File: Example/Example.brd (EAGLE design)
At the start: 86 x 54 mm, 25 parts, among them IC2 74LS02D, IC3 74LS02D, U1 CD4017

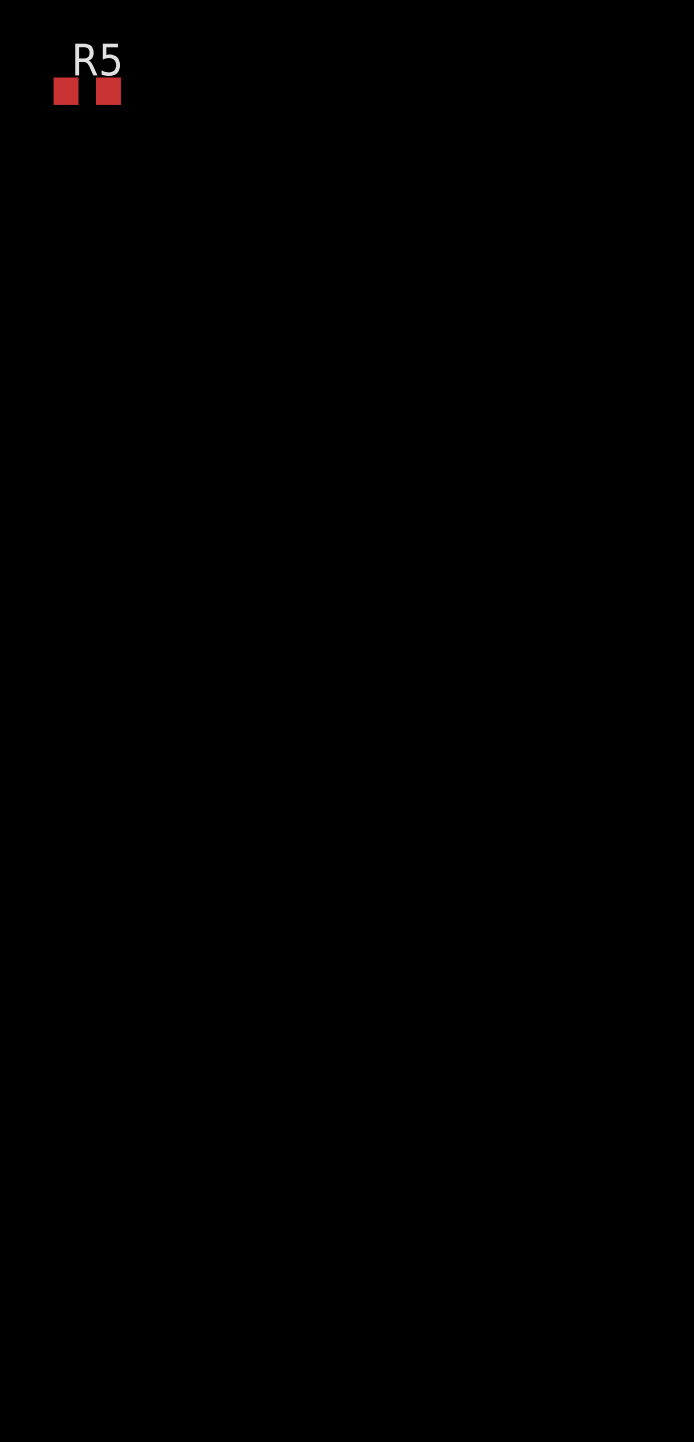
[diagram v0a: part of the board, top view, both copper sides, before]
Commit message: decade counter
added clocks and EN
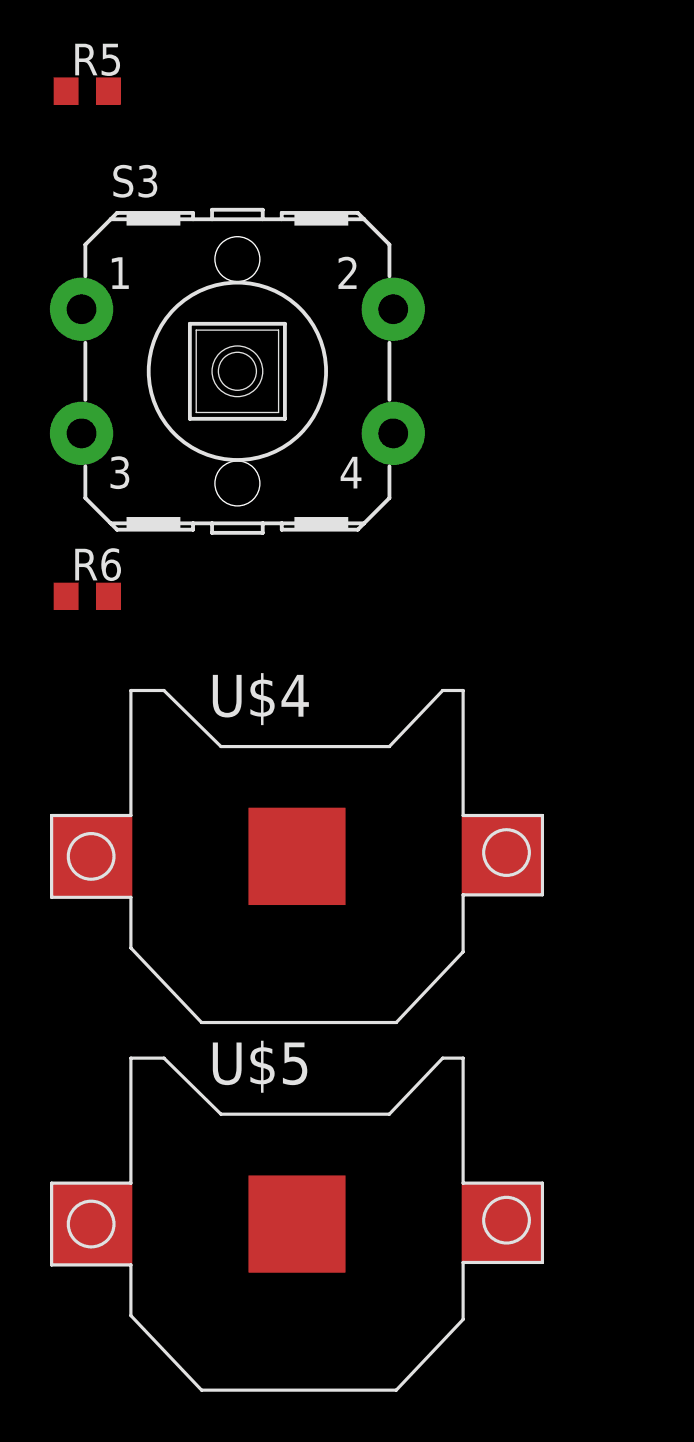
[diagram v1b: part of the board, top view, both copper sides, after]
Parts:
- added R6: 220, rcl:R0603
- added S3: (no value), adafruit:B3F-40XX-ROUND
- added U$4, U$5: (no value), adafruit:CR1220-SMD
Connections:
- new net N$1: R6.2, S3.2, U1.14
- net GND: now also R6.1, U$4.-, U$5.-, U1.13
- net VCC: now also U$4.+$1, U$5.+$1
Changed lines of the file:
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@@
 <attribute name="VALUE" x="-30.415" y="-147.805" size="1.27" layer="27"/>
+</element>
+<element name="S3" library="adafruit" library_urn="urn:adsk.eagle:library:420" package="B3F-40XX-ROUND" package3d_urn="urn:adsk.eagle:package:6240926/1" value="" x="-23.76" y="-157.13" smashed="yes">
+<attribute name="NAME" x="-28.84" y="-150.145" size="1.27" layer="25" ratio="10"/>
+<attribute name="VALUE" x="-26.935" y="-162.21" size="1.27" layer="27" ratio="10"/>
+</element>
+<element name="R6" library="rcl" library_urn="urn:adsk.eagle:library:334" package="R0603" package3d_urn="urn:adsk.eagle:package:23555/3" value="220" x="-29.78" y="-166.15" smashed="yes">
+<attribute name="NAME" x="-30.415" y="-165.515" size="1.27" layer="25"/>
+<attribute name="POPULARITY" value="77" x="-29.78" y="-166.15" size="1.778" layer="27" display="off"/>
+<attribute name="SPICEPREFIX" value="R" x="-29.78" y="-166.15" size="1.778" layer="27" display="off"/>
+<attribute name="VALUE" x="-30.415" y="-168.055" size="1.27" layer="27"/>
+</element>
+<element name="U$4" library="adafruit" library_urn="urn:adsk.eagle:library:420" package="CR1220-SMD" package3d_urn="urn:adsk.eagle:package:6240665/1" value="" x="-21.37" y="-176.58" smashed="yes">
+<attribute name="NAME" x="-24.926" y="-170.978" size="1.6764" layer="25" font="vector"/>
+<attribute name="VALUE" x="-25.688" y="-181.13" size="1.6764" layer="27" font="vector"/>
+</element>
+<element name="U$5" library="adafruit" library_urn="urn:adsk.eagle:library:420" package="CR1220-SMD" package3d_urn="urn:adsk.eagle:package:6240665/1" value="" x="-21.37" y="-191.32" smashed="yes">
+<attribute name="NAME" x="-24.926" y="-185.718" size="1.6764" layer="25" font="vector"/>
+<attribute name="VALUE" x="-25.688" y="-195.87" size="1.6764" layer="27" font="vector"/>
 </element>
 </elements>
@@
 <contactref element="R4" pad="1"/>
 <contactref element="R5" pad="1"/>
+<contactref element="R6" pad="1"/>
+<contactref element="U$4" pad="-"/>
+<contactref element="U$5" pad="-"/>
+<contactref element="U1" pad="13"/>
+<wire x1="-21.37" y1="-176.58" x2="-21.37" y2="-191.32" width="0" layer="19" extent="1-1"/>
+<wire x1="-30.63" y1="-166.15" x2="-21.37" y2="-176.58" width="0" layer="19" extent="1-1"/>
+<wire x1="-30.63" y1="-145.9" x2="-30.63" y2="-166.15" width="0" layer="19" extent="1-1"/>
 <wire x1="-30.63" y1="-141.02" x2="-30.63" y2="-145.9" width="0" layer="19" extent="1-1"/>
-<wire x1="-21.37" y1="-79.78" x2="-30.63" y2="-141.02" width="0" layer="19" extent="1-1"/>
+<wire x1="-20.84" y1="-87.32" x2="-30.63" y2="-141.02" width="0" layer="19" extent="1-1"/>
+<wire x1="-21.37" y1="-79.78" x2="-20.84" y2="-87.32" width="0" layer="19" extent="1-1"/>
 <wire x1="-30.63" y1="-70.74" x2="-21.37" y2="-79.78" width="0" layer="19" extent="1-1"/>
 <wire x1="-30.63" y1="-67.26" x2="-30.63" y2="-70.74" width="0" layer="19" extent="1-1"/>
@@
 <contactref element="U$1" pad="+$1"/>
 <contactref element="U$3" pad="+$1"/>
+<contactref element="U$4" pad="+$1"/>
+<contactref element="U$5" pad="+$1"/>
+<wire x1="-29.57" y1="-176.58" x2="-29.57" y2="-191.32" width="0" layer="19" extent="1-1"/>
+<wire x1="-29.57" y1="-79.78" x2="-29.57" y2="-176.58" width="0" layer="19" extent="1-1"/>
 <wire x1="-30.0084" y1="-60.7292" x2="-29.57" y2="-79.78" width="0" layer="19" extent="1-1"/>
 <wire x1="-14.18" y1="-29.9966" x2="-30.0084" y2="-60.7292" width="0" layer="19" extent="1-1"/>
@@
 <wire x1="-25.92" y1="-87.32" x2="-28.93" y2="-145.9" width="0" layer="19" extent="1-1"/>
 </signal>
+<signal name="N$1">
+<contactref element="S3" pad="2"/>
+<contactref element="R6" pad="2"/>
+<contactref element="U1" pad="14"/>
+<wire x1="-17.5116" y1="-154.6408" x2="-28.93" y2="-166.15" width="0" layer="19" extent="1-1"/>
+<wire x1="-23.38" y1="-87.32" x2="-17.5116" y2="-154.6408" width="0" layer="19" extent="1-1"/>
+</signal>
 </signals>

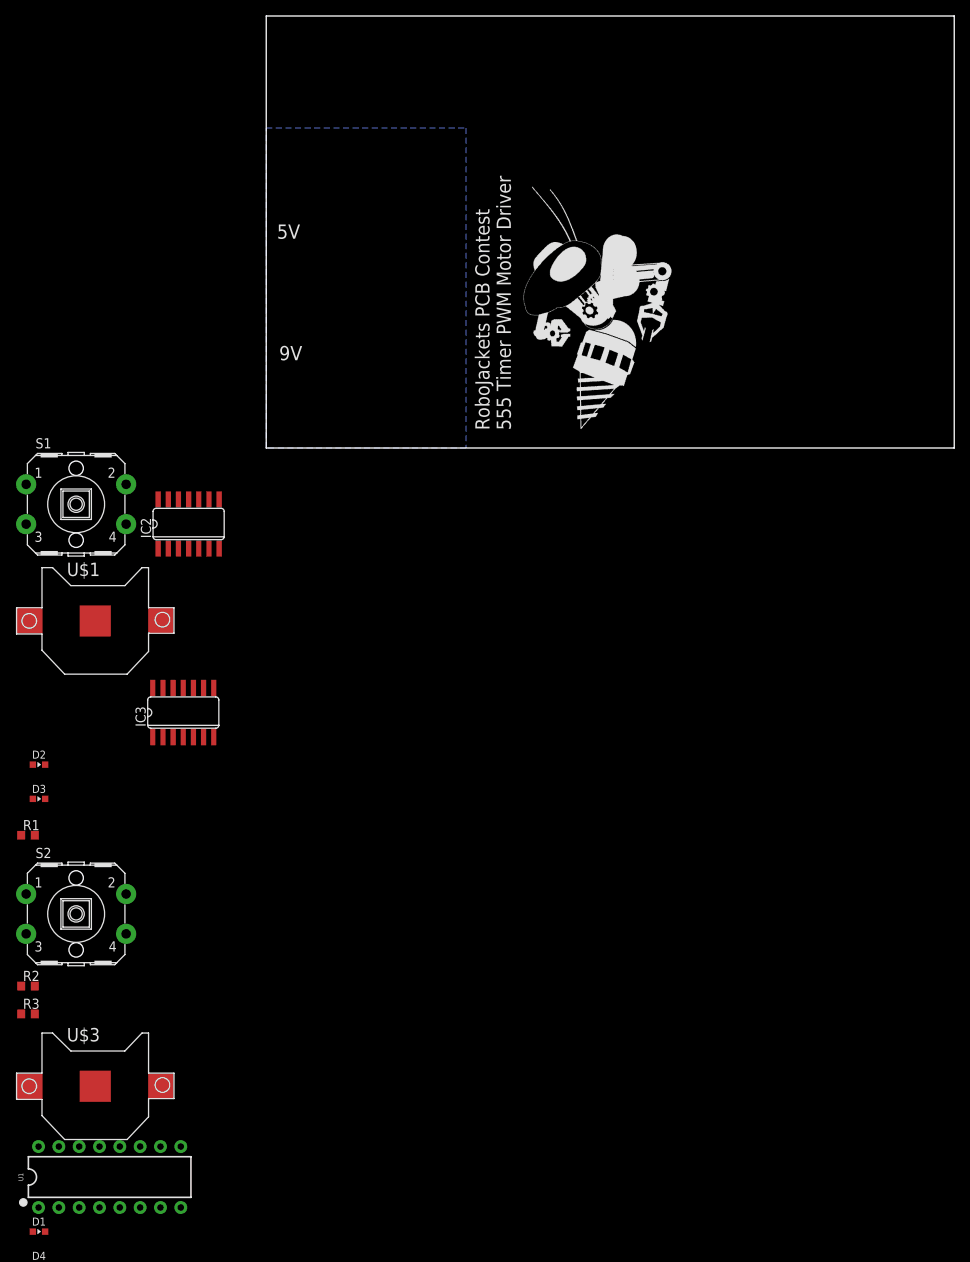
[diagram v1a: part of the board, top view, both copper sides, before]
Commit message: Fixed multiple NOR gate issue
Removed IC3A from the schematic
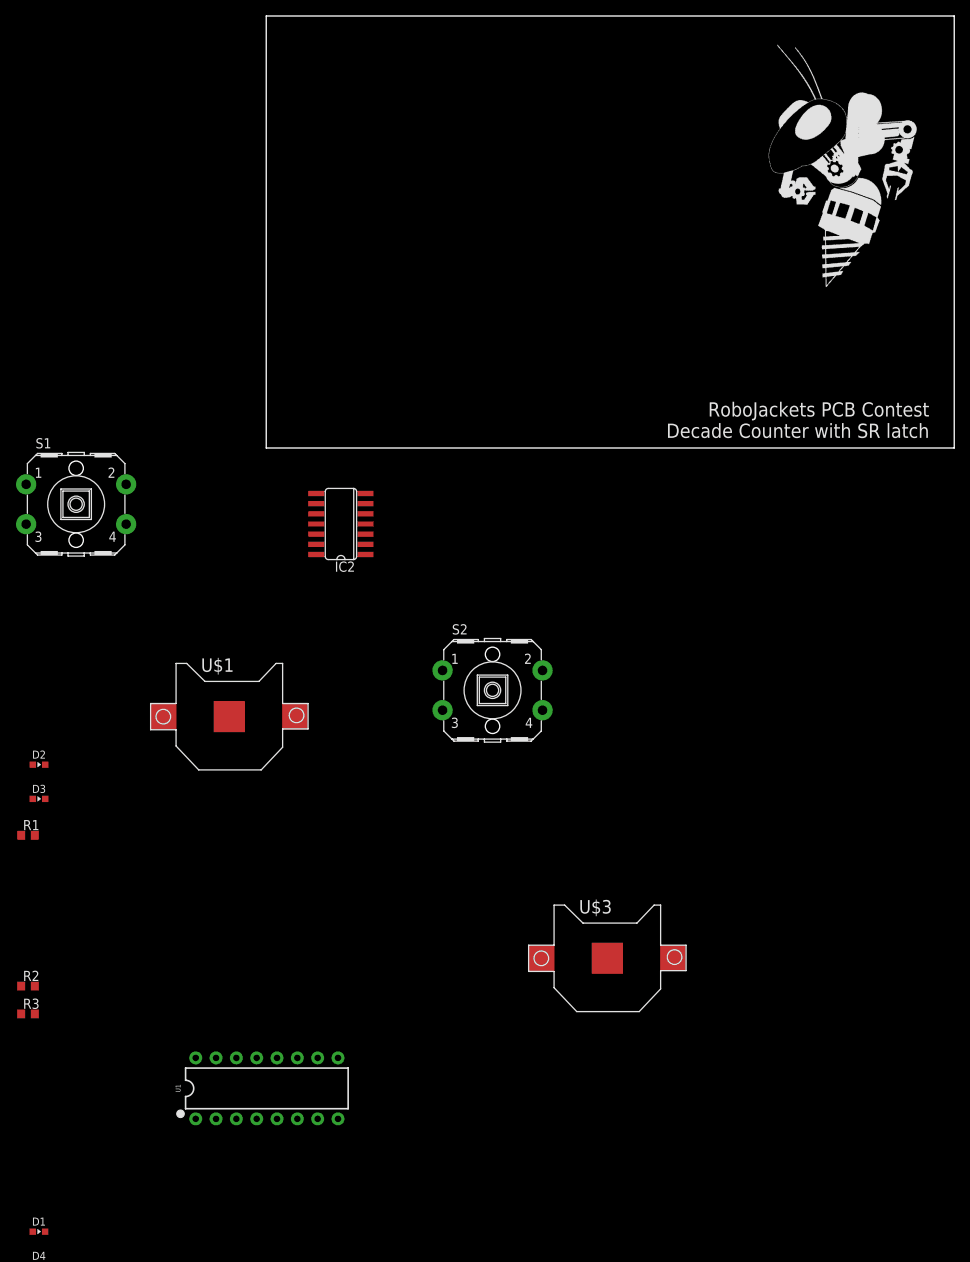
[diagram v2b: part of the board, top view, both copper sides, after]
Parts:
- removed IC3: 74LS02D, 74xx-us:SO14
- moved U$3 66.0 mm to (42.6, -63.8)
- moved S2 59.1 mm to (28.3, -30.3)
- moved U$2 35.4 mm to (69.9, 20.1)
- moved U1 22.6 mm to (0.08, -80.0)
- moved U$1 20.6 mm to (-4.61, -33.6)
- moved IC2 19.0 mm to (9.34, -9.50), turned to 90 degrees
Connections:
- removed net N$7: IC2.5
- removed net N$8: IC2.4
- removed net N$9: IC2.6
- net GND: no longer IC3.7
- net Q: now also IC2.5; no longer IC3.2
- net QNOT: now also IC2.4; no longer IC3.1
- net S: now also IC2.6; no longer IC3.3
- net VCC: no longer IC3.14
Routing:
- removed copper zone on layer 16, net GND
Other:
- board text added: "RoboJackets PCB Contest Decade Counter with SR latch"
- board text removed: "5V"
- board text removed: "9V"
- board text removed: "RoboJackets PCB Contest 555 Timer PWM Motor Driver"

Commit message: placed items on board
i placed everything on the board except for battery holders
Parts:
- removed D2: YELLOW, RoboJackets-LEDs:LED0603
- moved R6 192.5 mm to (45.6, 11.0)
- moved S3 178.0 mm to (31.9, 11.9)
- moved R5 177.5 mm to (45.5, 14.8)
- moved U$4 176.5 mm to (52.9, -16.4)
- moved U$5 171.5 mm to (52.8, -36.7)
- moved D1 170.4 mm to (57.5, 49.3)
- moved D4 170.4 mm to (57.5, 45.0)
- moved D5 170.4 mm to (57.5, 40.7)
- moved D6 170.4 mm to (57.5, 36.4)
- moved D10 170.4 mm to (57.5, 19.3)
- moved D11 170.4 mm to (57.5, 15.0)
- moved D12 170.4 mm to (57.5, 10.8)
- moved D7 170.4 mm to (57.5, 32.2)
- moved D8 170.4 mm to (57.5, 27.9)
- moved D9 170.4 mm to (57.5, 23.6)
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
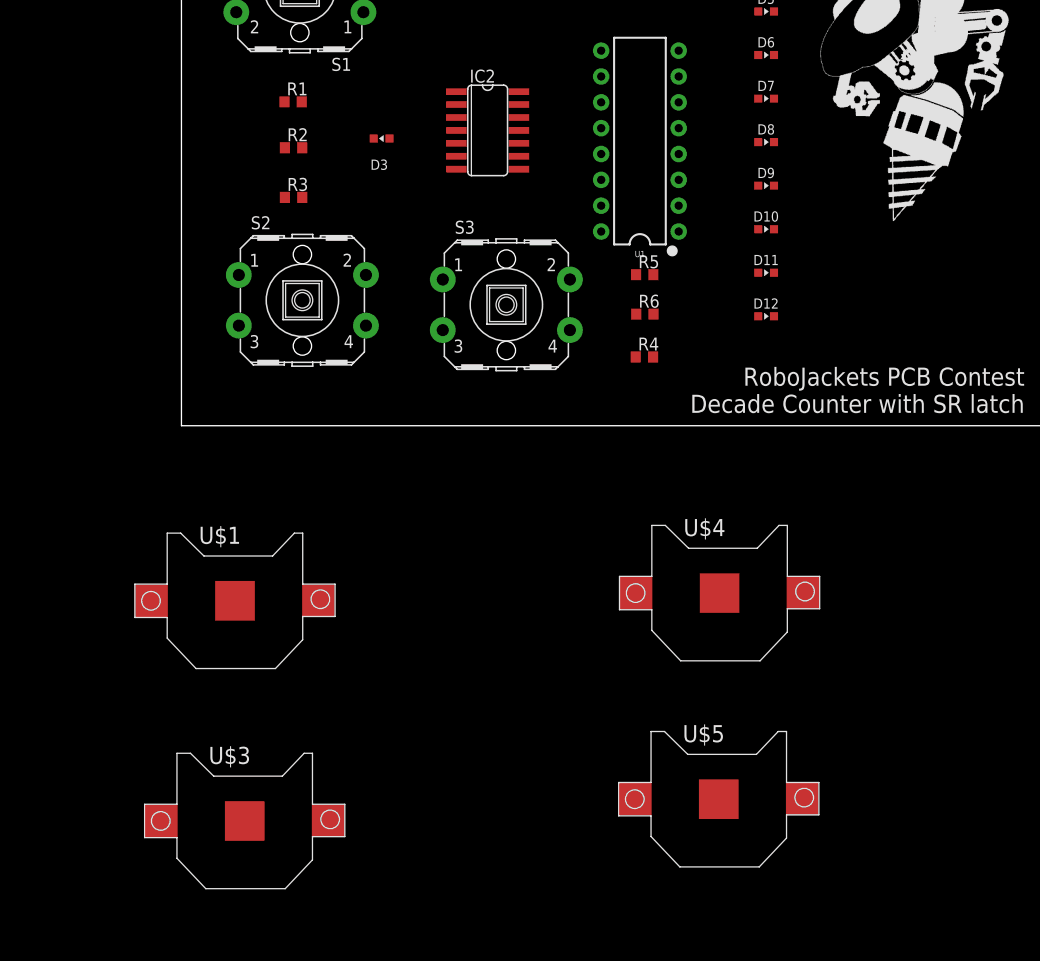
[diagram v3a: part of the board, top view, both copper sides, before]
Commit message: Added LEDs, made one Vcc, and updated board
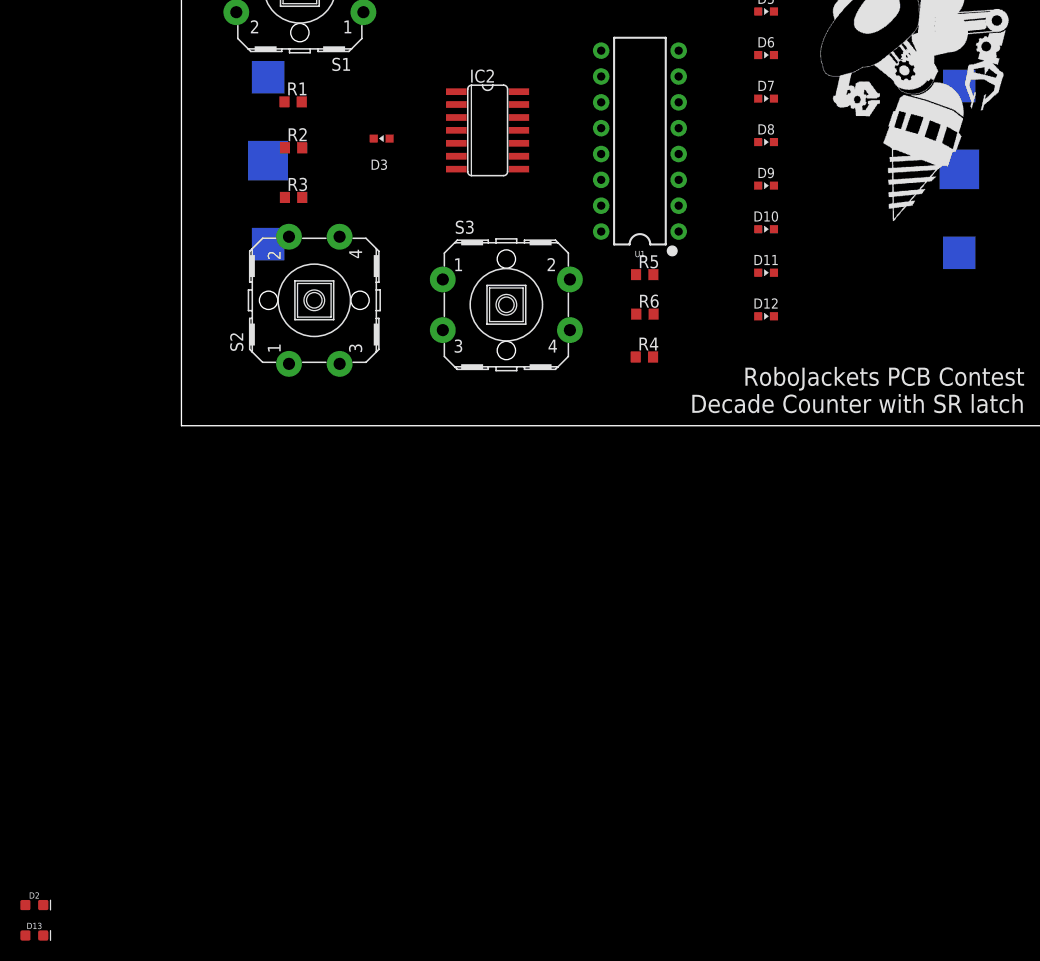
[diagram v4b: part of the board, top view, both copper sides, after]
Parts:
- removed U$4, U$5: (no value), adafruit:CR1220-SMD
- added D13: GREEN, RoboJackets-LEDs:LED-0603
- added D2: BLUE, RoboJackets-LEDs:LED-0603
- moved U$3 95.1 mm to (76.5, 25.2), flipped to the bottom, turned to 270 degrees
- moved U$1 43.4 mm to (8.52, 26.1), flipped to the bottom, turned to 90 degrees
- moved S2 1.17 mm to (13.1, 12.3), turned to 90 degrees
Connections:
- removed net N$1: R6.2, S3.2, U1.14
- net GND: no longer U$4.-, U$5.-
- net Q: now also R6.2, U1.14
- net VCC: no longer U$4.+$1, U$5.+$1
